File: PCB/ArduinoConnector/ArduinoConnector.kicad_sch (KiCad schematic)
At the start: 5 parts, among them J1 Arduino, J2 FAN, Q1 Q_NPN_EBC

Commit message: New PCBs
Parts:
- removed Q1: Q_NPN_EBC, symbol Device:Q_NPN_EBC
- added Q1: MMBT100, Package_TO_SOT_SMD:SOT-23, symbol Transistor_BJT:MMBTA42
- D1: value 1N4001 -> 1N5819; footprint Diode_THT:D_DO-41_SOD81_P10.16mm_Horizontal -> Diode_SMD:D_SMA
- J1: footprint (none) -> Connector_PinHeader_2.54mm:PinHeader_2x03_P2.54mm_Vertical
- J2: footprint (none) -> Connector_Molex:Molex_KK-254_AE-6410-04A_1x04_P2.54mm_Vertical
- R1: footprint (none) -> Resistor_SMD:R_0805_2012Metric
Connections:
- net +5V: now also J2.2 (Pin_2); no longer J2.3 (Pin_3)
- net FAN_GND: now also J2.1 (Pin_1), Q1.3 (C); no longer J2.4 (Pin_4)
- net GND: now also Q1.2 (E)
- net PWM: now also J2.4 (Pin_4); no longer J2.1 (Pin_1)
- net SENSE: now also J2.3 (Pin_3); no longer J2.2 (Pin_2)
- net at R1.2: now also Q1.1 (B)
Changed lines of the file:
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@@
     (property "Reference" "R1" (id 0) (at 121.92 94.0775 90))
     (property "Value" "330" (id 1) (at 121.92 96.8526 90))
-    (property "Footprint" "" (id 2) (at 121.92 100.838 90)
+    (property "Footprint" "Resistor_SMD:R_0805_2012Metric" (id 2) (at 121.92 100.838 90)
       (effects (font (size 1.27 1.27)) hide)
     )
@@
     (pin "1")
     (pin "2")
-  )
-  (symbol (lib_id "Device:Q_NPN_EBC") (at 134.62 99.06 0) (unit 1)
-    (in_bom yes) (on_board yes) (fields_autoplaced)
-    (property "Reference" "Q1" (id 0) (at 139.4714 98.1515 0)
-      (effects (font (size 1.27 1.27)) (justify left))
-    )
-    (property "Value" "Q_NPN_EBC" (id 1) (at 139.4714 100.9266 0)
-      (effects (font (size 1.27 1.27)) (justify left))
-    )
-    (property "Footprint" "" (id 2) (at 139.7 96.52 0)
-      (effects (font (size 1.27 1.27)) hide)
-    )
-    (property "Datasheet" "~" (id 3) (at 134.62 99.06 0)
-      (effects (font (size 1.27 1.27)) hide)
-    )
-    (pin "1")
-    (pin "2")
-    (pin "3")
   )
   (symbol (lib_id "power:PWR_FLAG") (at 146.05 62.23 0) (mirror y) (unit 1)
@@
       (effects (font (size 1.27 1.27)) (justify left))
     )
-    (property "Value" "1N4001" (id 1) (at 139.192 85.6866 90)
+    (property "Value" "1N5819" (id 1) (at 139.192 85.6866 90)
       (effects (font (size 1.27 1.27)) (justify left))
     )
-    (property "Footprint" "Diode_THT:D_DO-41_SOD81_P10.16mm_Horizontal" (id 2) (at 132.715 83.82 0)
+    (property "Footprint" "Diode_SMD:D_SMA" (id 2) (at 132.715 83.82 0)
       (effects (font (size 1.27 1.27)) hide)
     )
@@
     (pin "1")
   )
-  (symbol (lib_id "Connector_Generic:Conn_01x04") (at 180.34 85.09 0) (unit 1)
+  (symbol (lib_id "Connector_Generic:Conn_01x04") (at 180.34 87.63 0) (mirror x) (unit 1)
     (in_bom yes) (on_board yes) (fields_autoplaced)
-    (property "Reference" "J2" (id 0) (at 182.372 85.4515 0)
-      (effects (font (size 1.27 1.27)) (justify left))
-    )
-    (property "Value" "FAN" (id 1) (at 182.372 88.2266 0)
-      (effects (font (size 1.27 1.27)) (justify left))
-    )
-    (property "Footprint" "" (id 2) (at 180.34 85.09 0)
+    (property "Reference" "J2" (id 0) (at 180.34 77.3135 0))
+    (property "Value" "FAN" (id 1) (at 180.34 80.0886 0))
+    (property "Footprint" "Connector_Molex:Molex_KK-254_AE-6410-04A_1x04_P2.54mm_Vertical" (id 2) (at 180.34 87.63 0)
       (effects (font (size 1.27 1.27)) hide)
     )
-    (property "Datasheet" "~" (id 3) (at 180.34 85.09 0)
+    (property "Datasheet" "~" (id 3) (at 180.34 87.63 0)
       (effects (font (size 1.27 1.27)) hide)
     )
@@
     (pin "3")
     (pin "4")
+  )
+  (symbol (lib_id "Transistor_BJT:MMBTA42") (at 134.62 99.06 0) (unit 1)
+    (in_bom yes) (on_board yes) (fields_autoplaced)
+    (property "Reference" "Q1" (id 0) (at 139.4714 98.1515 0)
+      (effects (font (size 1.27 1.27)) (justify left))
+    )
+    (property "Value" "MMBT100" (id 1) (at 139.4714 100.9266 0)
+      (effects (font (size 1.27 1.27)) (justify left))
+    )
+    (property "Footprint" "Package_TO_SOT_SMD:SOT-23" (id 2) (at 139.7 100.965 0)
+      (effects (font (size 1.27 1.27) italic) (justify left) hide)
+    )
+    (property "Datasheet" "https://www.onsemi.com/pub/Collateral/MMBTA42LT1-D.PDF" (id 3) (at 134.62 99.06 0)
+      (effects (font (size 1.27 1.27)) (justify left) hide)
+    )
+    (pin "1")
+    (pin "2")
+    (pin "3")
   )
   (symbol (lib_id "power:PWR_FLAG") (at 127 109.22 180) (unit 1)
@@
     (property "Reference" "J1" (id 0) (at 90.17 78.5835 0))
     (property "Value" "Arduino" (id 1) (at 90.17 81.3586 0))
-    (property "Footprint" "" (id 2) (at 88.9 86.36 0)
+    (property "Footprint" "Connector_PinHeader_2.54mm:PinHeader_2x03_P2.54mm_Vertical" (id 2) (at 88.9 86.36 0)
       (effects (font (size 1.27 1.27)) hide)
     )
@@
     )
     (path "/796618ff-adc1-4daf-832e-9d9cc9a2585a"
-      (reference "D1") (unit 1) (value "1N4001") (footprint "Diode_THT:D_DO-41_SOD81_P10.16mm_Horizontal")
+      (reference "D1") (unit 1) (value "1N5819") (footprint "Diode_SMD:D_SMA")
     )
     (path "/d6040293-95f0-436a-938c-ad69875a4be8"
-      (reference "J1") (unit 1) (value "Arduino") (footprint "")
+      (reference "J1") (unit 1) (value "Arduino") (footprint "Connector_PinHeader_2.54mm:PinHeader_2x03_P2.54mm_Vertical")
     )
     (path "/9661476a-e3cc-43ad-bbdf-24b6874ef400"
-      (reference "J2") (unit 1) (value "FAN") (footprint "")
+      (reference "J2") (unit 1) (value "FAN") (footprint "Connector_Molex:Molex_KK-254_AE-6410-04A_1x04_P2.54mm_Vertical")
     )
-    (path "/48e8d634-1608-4cd1-814c-418fcd84837c"
-      (reference "Q1") (unit 1) (value "Q_NPN_EBC") (footprint "")
+    (path "/a83bc339-0e58-46db-b9d7-1089d0fbf78b"
+      (reference "Q1") (unit 1) (value "MMBT100") (footprint "Package_TO_SOT_SMD:SOT-23")
     )
     (path "/4400a03f-43f5-4fdb-be50-2ac899677f37"
-      (reference "R1") (unit 1) (value "330") (footprint "")
+      (reference "R1") (unit 1) (value "330") (footprint "Resistor_SMD:R_0805_2012Metric")
     )
   )

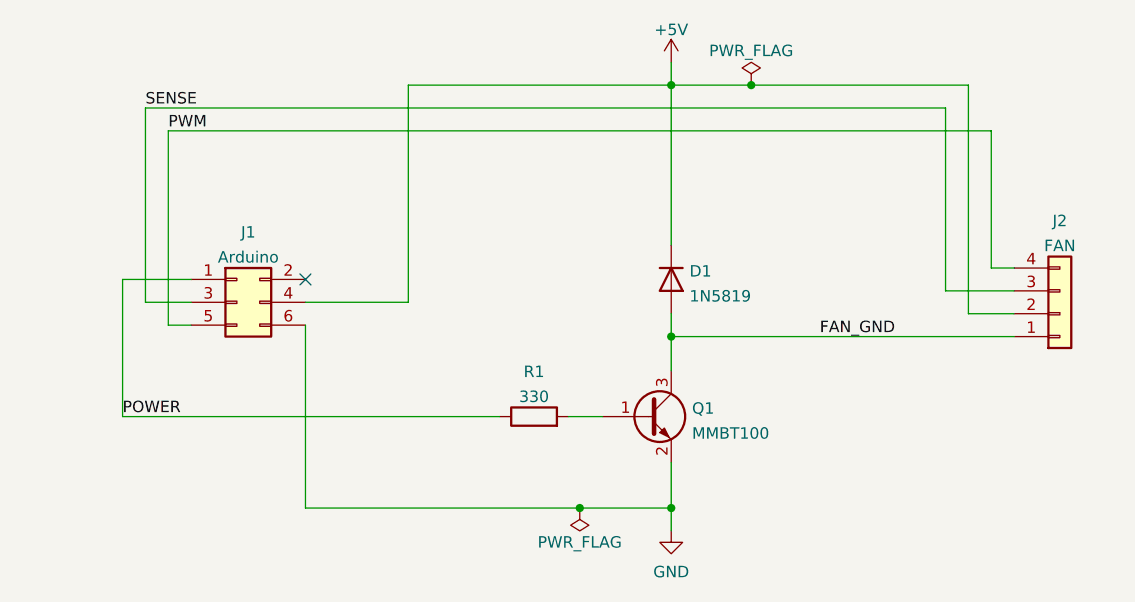
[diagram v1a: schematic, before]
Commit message: Changed pin assignments and redid the PCB
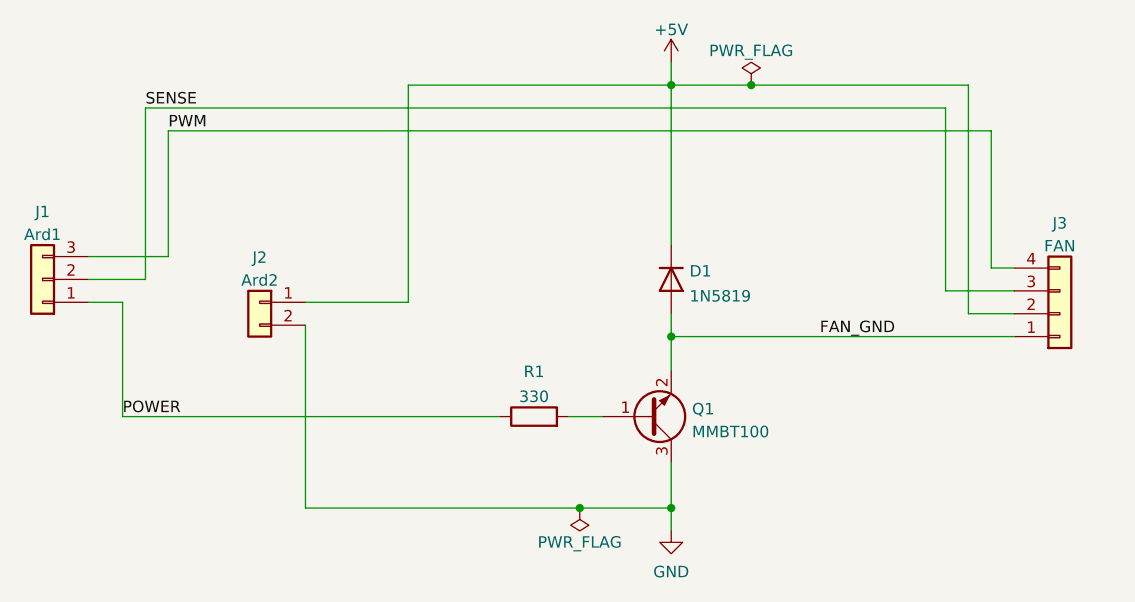
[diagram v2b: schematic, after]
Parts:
- removed J1: Arduino, Connector_PinHeader_2.54mm:PinHeader_2x03_P2.54mm_Vertical, symbol Connector_Generic:Conn_02x03_Odd_Even
- added J1: Ard1, Connector_PinHeader_2.54mm:PinHeader_1x03_P2.54mm_Vertical, symbol Connector_Generic:Conn_01x03
- added J2: Ard2, Connector_PinHeader_2.54mm:PinHeader_1x02_P2.54mm_Vertical, symbol Connector_Generic:Conn_01x02
- renumbered J2 to J3
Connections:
- net +5V: now also J2.1 (Pin_1)
- net FAN_GND: now also Q1.2 (E); no longer Q1.3 (C)
- net GND: now also Q1.3 (C), J2.2 (Pin_2); no longer Q1.2 (E)
- net POWER: now also J1.1 (Pin_1)
- net PWM: now also J1.3 (Pin_3)
- net SENSE: now also J1.2 (Pin_2)
- no-connect marks 1 -> 0
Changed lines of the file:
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@@
     (title "ArduinoConnector")
     (date "2022-03-11")
-    (rev "1")
+    (rev "2")
   )
   (junction (at 137.16 62.23) (diameter 0) (color 0 0 0 0)
@@
   (junction (at 137.16 90.17) (diameter 0) (color 0 0 0 0)
   )
-  (no_connect (at 96.52 83.82))
   (wire (pts (xy 96.52 109.22) (xy 127 109.22))
     (stroke (width 0) (type default) (color 0 0 0 0))
   )
+  (wire (pts (xy 72.39 81.28) (xy 81.28 81.28))
+    (stroke (width 0) (type default) (color 0 0 0 0))
+  )
+  (wire (pts (xy 72.39 86.36) (xy 76.2 86.36))
+    (stroke (width 0) (type default) (color 0 0 0 0))
+  )
   (wire (pts (xy 96.52 88.9) (xy 96.52 109.22))
     (stroke (width 0) (type default) (color 0 0 0 0))
@@
     (stroke (width 0) (type default) (color 0 0 0 0))
   )
+  (wire (pts (xy 76.2 86.36) (xy 76.2 99.06))
+    (stroke (width 0) (type default) (color 0 0 0 0))
+  )
   (wire (pts (xy 172.72 67.31) (xy 172.72 82.55))
     (stroke (width 0) (type default) (color 0 0 0 0))
   )
-  (wire (pts (xy 76.2 83.82) (xy 76.2 99.06))
-    (stroke (width 0) (type default) (color 0 0 0 0))
-  )
   (wire (pts (xy 137.16 90.17) (xy 175.26 90.17))
     (stroke (width 0) (type default) (color 0 0 0 0))
@@
     (stroke (width 0) (type default) (color 0 0 0 0))
   )
-  (wire (pts (xy 78.74 64.77) (xy 78.74 86.36))
-    (stroke (width 0) (type default) (color 0 0 0 0))
-  )
-  (wire (pts (xy 83.82 83.82) (xy 76.2 83.82))
+  (wire (pts (xy 78.74 64.77) (xy 78.74 83.82))
+    (stroke (width 0) (type default) (color 0 0 0 0))
+  )
+  (wire (pts (xy 72.39 83.82) (xy 78.74 83.82))
     (stroke (width 0) (type default) (color 0 0 0 0))
   )
@@
     (stroke (width 0) (type default) (color 0 0 0 0))
   )
-  (wire (pts (xy 78.74 86.36) (xy 83.82 86.36))
-    (stroke (width 0) (type default) (color 0 0 0 0))
-  )
-  (wire (pts (xy 83.82 88.9) (xy 81.28 88.9))
+  (wire (pts (xy 81.28 81.28) (xy 81.28 67.31))
     (stroke (width 0) (type default) (color 0 0 0 0))
   )
   (wire (pts (xy 137.16 90.17) (xy 137.16 93.98))
-    (stroke (width 0) (type default) (color 0 0 0 0))
-  )
-  (wire (pts (xy 81.28 88.9) (xy 81.28 67.31))
     (stroke (width 0) (type default) (color 0 0 0 0))
   )
@@
     (pin "2")
   )
+  (symbol (lib_id "Connector_Generic:Conn_01x02") (at 91.44 86.36 0) (mirror y) (unit 1)
+    (in_bom yes) (on_board yes) (fields_autoplaced)
+    (property "Reference" "J2" (id 0) (at 91.44 81.3902 0))
+    (property "Value" "Ard2" (id 1) (at 91.44 83.9271 0))
+    (property "Footprint" "Connector_PinHeader_2.54mm:PinHeader_1x02_P2.54mm_Vertical" (id 2) (at 91.44 86.36 0)
+      (effects (font (size 1.27 1.27)) hide)
+    )
+    (property "Datasheet" "~" (id 3) (at 91.44 86.36 0)
+      (effects (font (size 1.27 1.27)) hide)
+    )
+    (pin "1")
+    (pin "2")
+  )
   (symbol (lib_id "power:PWR_FLAG") (at 146.05 62.23 0) (mirror y) (unit 1)
     (in_bom yes) (on_board yes)
@@
     (pin "1")
   )
+  (symbol (lib_id "Connector_Generic:Conn_01x03") (at 67.31 83.82 180) (unit 1)
+    (in_bom yes) (on_board yes) (fields_autoplaced)
+    (property "Reference" "J1" (id 0) (at 67.31 76.3102 0))
+    (property "Value" "Ard1" (id 1) (at 67.31 78.8471 0))
+    (property "Footprint" "Connector_PinHeader_2.54mm:PinHeader_1x03_P2.54mm_Vertical" (id 2) (at 67.31 83.82 0)
+      (effects (font (size 1.27 1.27)) hide)
+    )
+    (property "Datasheet" "~" (id 3) (at 67.31 83.82 0)
+      (effects (font (size 1.27 1.27)) hide)
+    )
+    (pin "1")
+    (pin "2")
+    (pin "3")
+  )
   (symbol (lib_id "Connector_Generic:Conn_01x04") (at 180.34 87.63 0) (mirror x) (unit 1)
     (in_bom yes) (on_board yes) (fields_autoplaced)
-    (property "Reference" "J2" (id 0) (at 180.34 77.3135 0))
-    (property "Value" "FAN" (id 1) (at 180.34 80.0886 0))
+    (property "Reference" "J3" (id 0) (at 180.34 77.5802 0))
+    (property "Value" "FAN" (id 1) (at 180.34 80.1171 0))
     (property "Footprint" "Connector_Molex:Molex_KK-254_AE-6410-04A_1x04_P2.54mm_Vertical" (id 2) (at 180.34 87.63 0)
       (effects (font (size 1.27 1.27)) hide)
@@
     (pin "4")
   )
-  (symbol (lib_id "Transistor_BJT:MMBTA42") (at 134.62 99.06 0) (unit 1)
-    (in_bom yes) (on_board yes) (fields_autoplaced)
-    (property "Reference" "Q1" (id 0) (at 139.4714 98.1515 0)
-      (effects (font (size 1.27 1.27)) (justify left))
-    )
-    (property "Value" "MMBT100" (id 1) (at 139.4714 100.9266 0)
-      (effects (font (size 1.27 1.27)) (justify left))
-    )
-    (property "Footprint" "Package_TO_SOT_SMD:SOT-23" (id 2) (at 139.7 100.965 0)
+  (symbol (lib_id "Transistor_BJT:MMBTA42") (at 134.62 99.06 0) (mirror x) (unit 1)
+    (in_bom yes) (on_board yes) (fields_autoplaced)
+    (property "Reference" "Q1" (id 0) (at 139.4714 98.2253 0)
+      (effects (font (size 1.27 1.27)) (justify left))
+    )
+    (property "Value" "MMBT100" (id 1) (at 139.4714 100.7622 0)
+      (effects (font (size 1.27 1.27)) (justify left))
+    )
+    (property "Footprint" "Package_TO_SOT_SMD:SOT-23" (id 2) (at 139.7 97.155 0)
       (effects (font (size 1.27 1.27) italic) (justify left) hide)
     )
@@
     (pin "1")
   )
-  (symbol (lib_id "Connector_Generic:Conn_02x03_Odd_Even") (at 88.9 86.36 0) (unit 1)
-    (in_bom yes) (on_board yes) (fields_autoplaced)
-    (property "Reference" "J1" (id 0) (at 90.17 78.5835 0))
-    (property "Value" "Arduino" (id 1) (at 90.17 81.3586 0))
-    (property "Footprint" "Connector_PinHeader_2.54mm:PinHeader_2x03_P2.54mm_Vertical" (id 2) (at 88.9 86.36 0)
-      (effects (font (size 1.27 1.27)) hide)
-    )
-    (property "Datasheet" "~" (id 3) (at 88.9 86.36 0)
-      (effects (font (size 1.27 1.27)) hide)
-    )
-    (pin "1")
-    (pin "2")
-    (pin "3")
-    (pin "4")
-    (pin "5")
-    (pin "6")
-  )
   (sheet_instances
     (path "/" (page "1"))
@@
       (reference "D1") (unit 1) (value "1N5819") (footprint "Diode_SMD:D_SMA")
     )
-    (path "/d6040293-95f0-436a-938c-ad69875a4be8"
-      (reference "J1") (unit 1) (value "Arduino") (footprint "Connector_PinHeader_2.54mm:PinHeader_2x03_P2.54mm_Vertical")
+    (path "/888c6fdf-c198-440a-97af-035b863dc875"
+      (reference "J1") (unit 1) (value "Ard1") (footprint "Connector_PinHeader_2.54mm:PinHeader_1x03_P2.54mm_Vertical")
+    )
+    (path "/55b28997-b330-40d1-b32a-125cd071668d"
+      (reference "J2") (unit 1) (value "Ard2") (footprint "Connector_PinHeader_2.54mm:PinHeader_1x02_P2.54mm_Vertical")
     )
     (path "/9661476a-e3cc-43ad-bbdf-24b6874ef400"
-      (reference "J2") (unit 1) (value "FAN") (footprint "Connector_Molex:Molex_KK-254_AE-6410-04A_1x04_P2.54mm_Vertical")
+      (reference "J3") (unit 1) (value "FAN") (footprint "Connector_Molex:Molex_KK-254_AE-6410-04A_1x04_P2.54mm_Vertical")
     )
     (path "/a83bc339-0e58-46db-b9d7-1089d0fbf78b"
